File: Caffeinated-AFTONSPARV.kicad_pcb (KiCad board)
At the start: 4 copper layers, 42.5 x 16.1 mm, 38 parts, among them J1 PWR, J2 LED, J3 TagConnect, J4 USB, Q1 AO3400A, Q2 AO3400A, Q3 AO3400A, SW1 SW_Push, U1 ESP32-C3-MINI-1-[H/N]4, U2 SY8201ABC

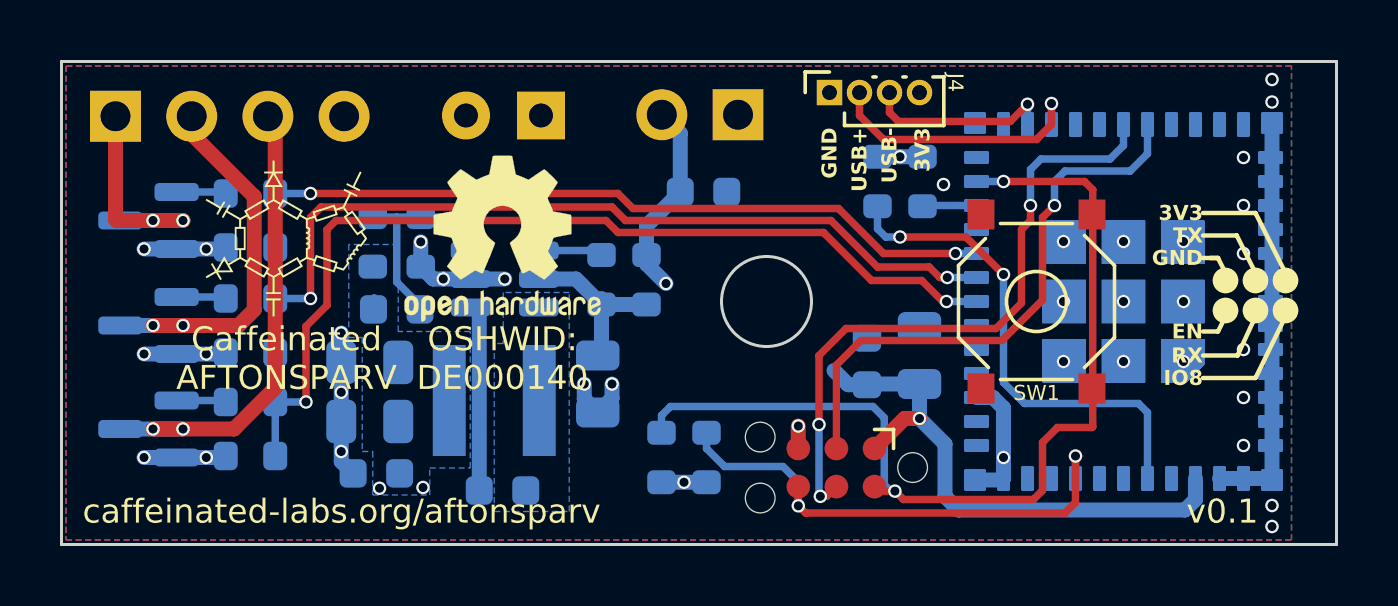
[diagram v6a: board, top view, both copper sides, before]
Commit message: fix(silkscreen): Add labels to all connections, correct errors and bump number
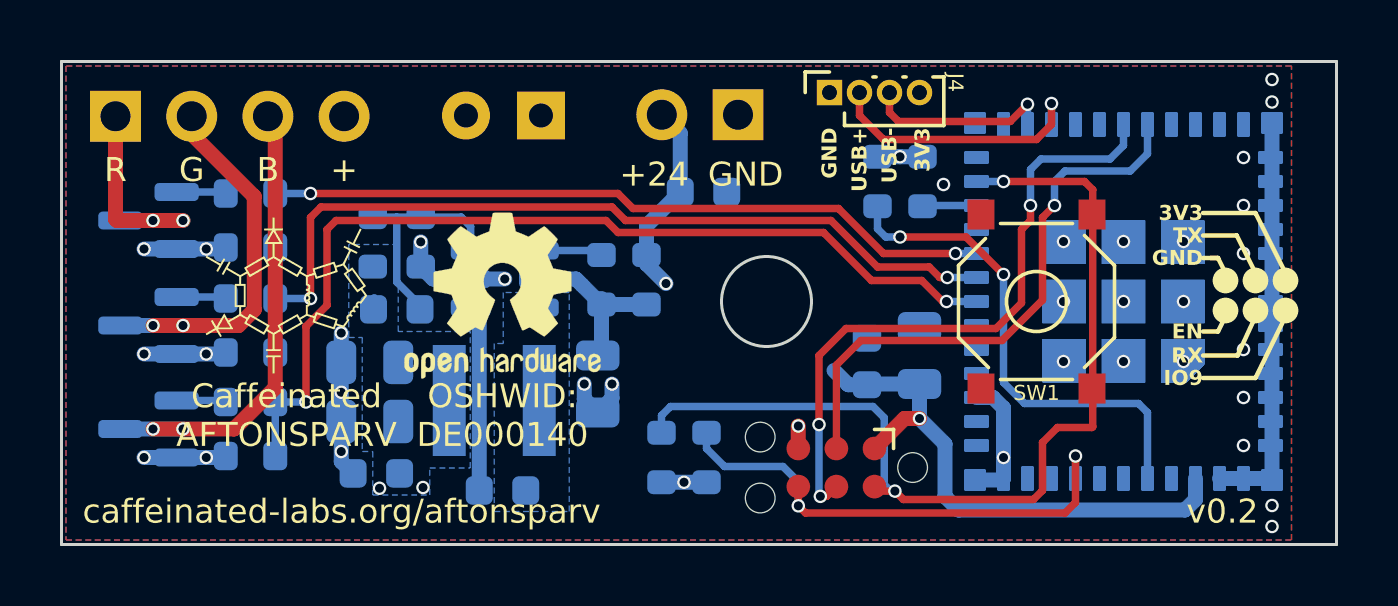
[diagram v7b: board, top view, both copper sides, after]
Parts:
- moved G*** 1.90 mm to (137.3, 99.8)
- moved REF** 1.90 mm to (144.5, 99.8)
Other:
- board text added: "+"
- board text added: "+24"
- board text added: "B"
- board text added: "G"
- board text added: "IO9"
- board text added: "R"
- board text added: "v0.2"
- board text removed: "IO8"
- board text removed: "v0.1"
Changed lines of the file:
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@@
     (pad_to_mask_clearance 0)
     (aux_axis_origin 129.8 108.1)
-    (grid_origin 153.3 100)
+    (grid_origin 152.35 93.775)
     (pcbplotparams
       (layerselection 0x00010fc_ffffffff)
@@
   )
   (footprint "LOGO" (layer "F.Cu")
-    (at 137.3 97.9)
+    (at 137.3 99.8)
     (attr board_only exclude_from_pos_files exclude_from_bom)
     (fp_text reference "G***" (at 0 0 unlocked) (layer "F.SilkS") hide
@@
   )
   (footprint "Symbol:OSHW-Logo2_7.3x6mm_SilkScreen" (layer "F.Cu")
-    (at 144.5 97.9)
+    (at 144.5 99.8)
     (descr "Open Source Hardware Symbol")
     (tags "Logo Symbol OSHW")
@@
     (effects (font (size 0.5 0.5) (thickness 0.1) bold) (justify right))
   )
-  (gr_text "IO8" (at 167.85 102.55) (layer "F.SilkS")
+  (gr_text "IO9" (at 167.85 102.55) (layer "F.SilkS")
     (effects (font (size 0.5 0.5) (thickness 0.1) bold) (justify right))
   )
-  (gr_text "Caffeinated\nAFTONSPARV" (at 137.3 101.9) (layer "F.SilkS")
+  (gr_text "+24" (at 149.556 95.299) (layer "F.SilkS")
+    (effects (font (size 0.8 0.8) (thickness 0.1)) (justify top))
+  )
+  (gr_text "+" (at 139.22 95.146) (layer "F.SilkS")
+    (effects (font (size 0.8 0.8) (thickness 0.1)) (justify top))
+  )
+  (gr_text "Caffeinated\nAFTONSPARV" (at 137.3 103.8) (layer "F.SilkS")
     (effects (font (size 0.8 0.8) (thickness 0.1)))
   )
-  (gr_text "OSHWID:\nDE000140" (at 144.5 101.9) (layer "F.SilkS")
+  (gr_text "OSHWID:\nDE000140" (at 144.5 103.8) (layer "F.SilkS")
     (effects (font (size 0.8 0.8) (thickness 0.1)))
   )
@@
     (effects (font (size 0.5 0.5) (thickness 0.1) bold) (justify right))
   )
-  (gr_text "v0.1" (at 167.3 107) (layer "F.SilkS")
+  (gr_text "B" (at 136.68 95.146) (layer "F.SilkS")
+    (effects (font (size 0.8 0.8) (thickness 0.1)) (justify top))
+  )
+  (gr_text "G" (at 134.14 95.146) (layer "F.SilkS")
+    (effects (font (size 0.8 0.8) (thickness 0.1)) (justify top))
+  )
+  (gr_text "v0.2" (at 167.3 107) (layer "F.SilkS")
     (effects (font (size 0.8 0.8) (thickness 0.1)) (justify left))
   )
@@
     (effects (font (size 0.5 0.5) (thickness 0.1) bold) (justify right))
   )
+  (gr_text "R" (at 131.6 95.146) (layer "F.SilkS")
+    (effects (font (size 0.8 0.8) (thickness 0.1)) (justify top))
+  )
   (gr_text "USB+" (at 156.4 94.2 90) (layer "F.SilkS")
     (effects (font (size 0.5 0.5) (thickness 0.1) bold) (justify right))
@@
     (effects (font (size 0.8 0.8) (thickness 0.1)) (justify left))
   )
+  (gr_text "GND" (at 152.604 95.299) (layer "F.SilkS")
+    (effects (font (size 0.8 0.8) (thickness 0.1)) (justify top))
+  )
   (gr_text "RX" (at 167.85 101.8) (layer "F.SilkS")
